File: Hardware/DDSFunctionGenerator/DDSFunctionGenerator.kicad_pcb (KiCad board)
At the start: 2 copper layers, 80 x 65 mm, 156 parts, among them J1 Conn_Coaxial, J2 USB_B_Micro, J3 DG128-5.0-02P-14-00A, J4 Conn_01x02_Female, J5 Conn_Coaxial, J6 Conn_Coaxial, J7 Conn_01x04_Male, J8 Conn_01x04_Female, J9 Conn_01x04_Female, Q1 Q_NPN_BEC, Q2 Q_NPN_BEC, Q3 Q_NPN_BEC, SW1 EN11-VSB1AQ15, T1 Transformer_1P_1S, U1 TC1107-3.3VOA, U2 L78L08_SOT89, U3 L78L33_SO8, U4 AD9832, U5 STM32F030K6Tx, U6 FT200XD, U7 AD8325, U8 MCP3425A0T-ECH, X1 XO91, Y1 20MHz

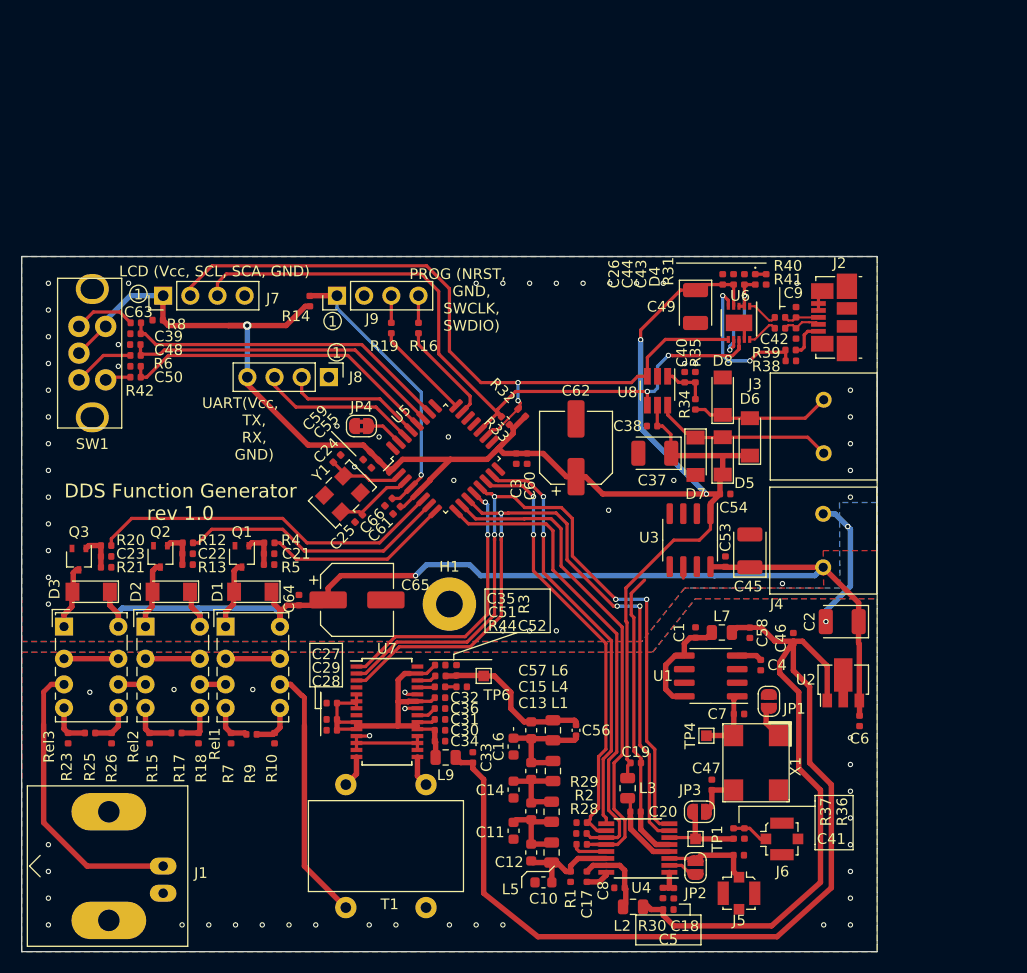
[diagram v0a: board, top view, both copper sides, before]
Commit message: move to raspbbery pico, first draft
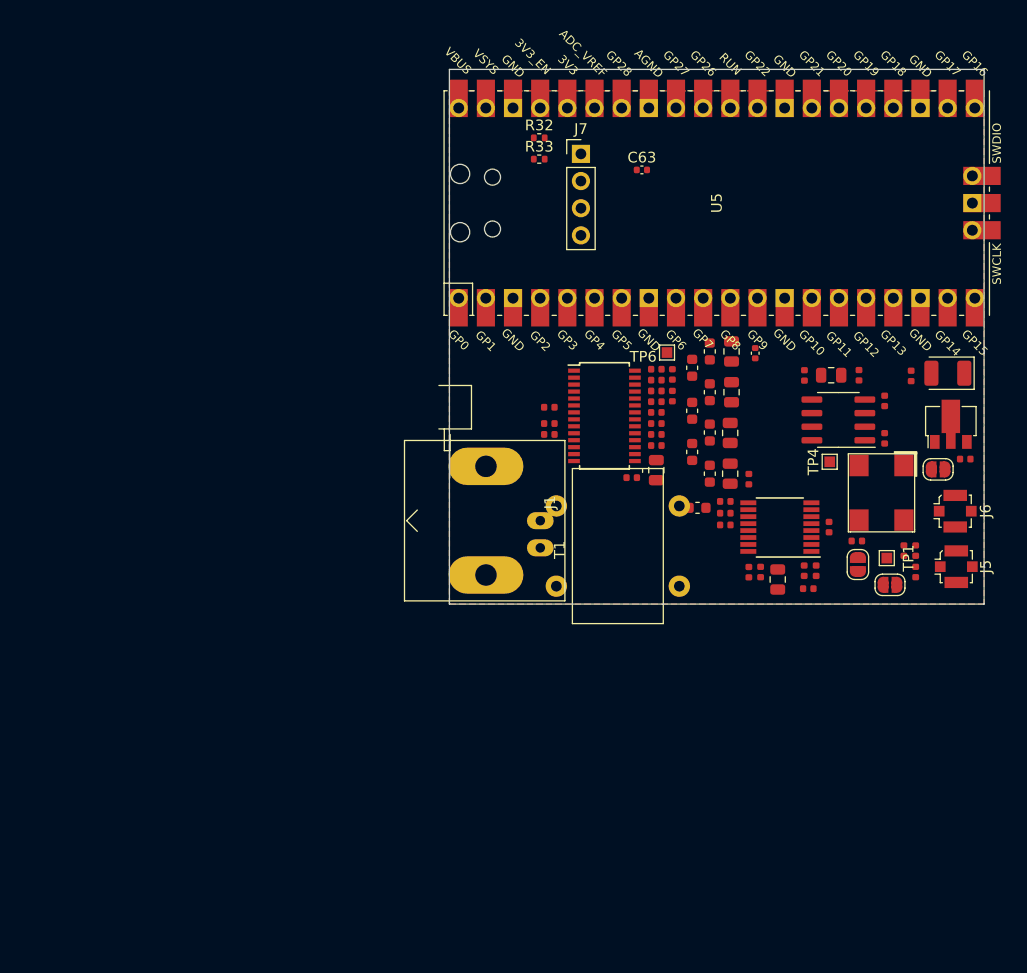
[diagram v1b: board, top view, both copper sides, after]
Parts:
- removed C19, C26, C3, C38, C43, C44, C50, C53, C54, C55, C59, C60, C61, C64, C66: 100n, Capacitor_SMD:C_0402_1005Metric
- removed C21, C22, C23, C40: 1n, Capacitor_SMD:C_0402_1005Metric
- removed C24, C25: 8p2, Capacitor_SMD:C_0402_1005Metric
- removed C37, C49: 47u/6V3, Capacitor_Tantalum_SMD:CP_EIA-3528-21_Kemet-B
- removed C39, C48: 10n, Capacitor_SMD:C_0402_1005Metric
- removed C42, C9: 47p, Capacitor_SMD:C_0402_1005Metric
- removed C45: 47u/10V, Capacitor_Tantalum_SMD:CP_EIA-3528-21_Kemet-B
- removed C62, C65: 220u, Capacitor_SMD:CP_Elec_6.3x5.8
- removed D1, D2, D3, D5, D6, D7, D8: D, Diode_SMD:D_MiniMELF
- removed D4: LED, LED_SMD:LED_0402_1005Metric
- removed H1: MountingHole_Pad, MountingHole:MountingHole_2.5mm_Pad
- removed J2: USB_B_Micro, Connector_USB:USB_Micro-B_Molex_47346-0001
- removed J3: DG128-5.0-02P-14-00A, DDSFunctionGenerator:DG128-5.0-02P-14-00A
- removed J4: Conn_01x02_Female, DDSFunctionGenerator:DG128-5.0-02P-14-00A
- removed J8, J9: Conn_01x04_Female, Connector_PinHeader_2.54mm:PinHeader_1x04_P2.54mm_Vertical
- removed JP4: Jumper_NC_Small, Jumper:SolderJumper-2_P1.3mm_Bridged2Bar_RoundedPad1.0x1.5mm
- removed L3: 10u, Inductor_SMD:L_0805_2012Metric
- removed Q1, Q2, Q3: Q_NPN_BEC, Package_TO_SOT_SMD:SOT-323_SC-70
- removed R10, R15, R18, R23, R26, R7: 53R6, Resistor_SMD:R_0402_1005Metric
- removed R12, R20, R4: 2k2, Resistor_SMD:R_0402_1005Metric
- removed R13, R14, R21, R35, R39, R5: 10k, Resistor_SMD:R_0402_1005Metric
- removed R16, R19: 220R, Resistor_SMD:R_0402_1005Metric
- removed R17, R25, R9: 1k, Resistor_SMD:R_0402_1005Metric
- removed R31: 120R, Resistor_SMD:R_0402_1005Metric
- removed R34: 0R, Resistor_SMD:R_0402_1005Metric
- removed R38: 4k7, Resistor_SMD:R_0402_1005Metric
- removed R40, R41: 27R, Resistor_SMD:R_0402_1005Metric
- removed R42, R6, R8: 100R, Resistor_SMD:R_0402_1005Metric
- removed Rel1, Rel2, Rel3: RSM850B-6112-85-1005, Relay_THT:Relay_DPDT_Omron_G6K-2P-Y
- removed SW1: EN11-VSB1AQ15, DDSFunctionGenerator:EN11-VNB1BQ15
- removed U3: L78L33_SO8, Package_SO:SOIC-8_3.9x4.9mm_P1.27mm
- removed U6: FT200XD, Package_DFN_QFN:DFN-10-1EP_3x3mm_P0.5mm_EP1.55x2.48mm
- removed U8: MCP3425A0T-ECH, Package_TO_SOT_SMD:SOT-23-6_Handsoldering
- removed Y1: 20MHz, Oscillator:Oscillator_SMD_EuroQuartz_XO53-4Pin_5.0x3.2mm
- U5: value STM32F030K6Tx -> RP2040; footprint Package_QFP:LQFP-32_7x7mm_P0.8mm -> MCU_RaspberryPi_and_Boards:RPi_Pico_SMD_TH
- moved J1 47.8 mm to (113.5, 94.7)
- moved C63 47.4 mm to (123.0, 61.9), turned to 0 degrees
- moved J7 41.3 mm to (117.3, 60.4), turned to 0 degrees
- moved R1 40.7 mm to (133.0, 90.8)
- moved C12 39.2 mm to (129.4, 90.3)
- moved L1 39.2 mm to (131.3, 86.5)
- moved L5 39.2 mm to (131.3, 90.3)
- moved L4 39.2 mm to (131.4, 82.7)
- moved L6 39.2 mm to (131.4, 78.9)
- moved C11 39.2 mm to (127.7, 88.3)
- moved C13 39.2 mm to (129.4, 86.5)
- moved C14 39.2 mm to (127.7, 84.4)
- moved C15 39.2 mm to (129.4, 82.7)
- moved C16 39.2 mm to (127.7, 80.4)
- moved C57 39.2 mm to (129.4, 78.9)
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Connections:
- C20 pad 1: Net-(C20-Pad1) -> 5V_DIGITAL
- J1 pad 1: Net-(J1-Pad1) -> (no net)
- T1 pad 3: RF_FROM_AMPLIFIER -> (no net)
- U4 pad 4: Net-(C20-Pad1) -> 5V_DIGITAL
- U4 pad 9: FSYNC -> (no net)
- U5 pad 1: 5V_DIGITAL -> unconnected-(U5-Pad1)
- U5 pad 10: PSEL0 -> unconnected-(U5-Pad10)
- U5 pad 11: SPI1_SCK -> unconnected-(U5-Pad11)
- U5 pad 12: SPI1_CS_AMPLIFIER -> unconnected-(U5-Pad12)
- U5 pad 13: SPI1_MOSI -> unconnected-(U5-Pad13)
- U5 pad 14: FSELECT -> unconnected-(U5-Pad14)
- U5 pad 15: FSYNC -> unconnected-(U5-Pad15)
- U5 pad 16: GND -> unconnected-(U5-Pad16)
- U5 pad 17: 5V_DIGITAL -> unconnected-(U5-Pad17)
- U5 pad 18: (no net) -> unconnected-(U5-Pad18)
- U5 pad 19: SCL -> unconnected-(U5-Pad19)
- U5 pad 2: Net-(C24-Pad2) -> unconnected-(U5-Pad2)
- U5 pad 20: SDA -> unconnected-(U5-Pad20)
- U5 pad 21: (no net) -> unconnected-(U5-Pad21)
- U5 pad 22: (no net) -> unconnected-(U5-Pad22)
- U5 pad 23: /Microcontroller/SWDIO -> unconnected-(U5-Pad23)
- U5 pad 24: /Microcontroller/SWCLK -> unconnected-(U5-Pad24)
- U5 pad 25: (no net) -> unconnected-(U5-Pad25)
- U5 pad 26: ROT_A -> unconnected-(U5-Pad26)
- U5 pad 27: ROT_A -> unconnected-(U5-Pad27)
- U5 pad 28: ROT_S -> unconnected-(U5-Pad28)
- U5 pad 29: /Microcontroller/USART_TX -> unconnected-(U5-Pad29)
- U5 pad 3: Net-(C25-Pad2) -> unconnected-(U5-Pad3)
- U5 pad 30: /Microcontroller/USART_RX -> unconnected-(U5-Pad30)
- U5 pad 31: Net-(JP4-Pad2) -> unconnected-(U5-Pad31)
- U5 pad 32: GND -> unconnected-(U5-Pad32)
- U5 pad 4: /Microcontroller/NRST -> unconnected-(U5-Pad4)
- U5 pad 5: 5V_DIGITAL -> unconnected-(U5-Pad5)
- U5 pad 6: REL_3 -> unconnected-(U5-Pad6)
- U5 pad 7: REL_2 -> unconnected-(U5-Pad7)
- U5 pad 8: REL_1 -> unconnected-(U5-Pad8)
- U5 pad 9: PSEL1 -> unconnected-(U5-Pad9)
- U7 pad 1: SPI1_CS_AMPLIFIER -> (no net)
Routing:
- net 5V_DIGITAL: track 175.4 -> 0.00 mm, vias 3 -> 0
- net 5V_ANALOG: track 132.0 -> 0.00 mm
- net 9V: track 112.2 -> 0.00 mm, vias 1 -> 0
- net SPI1_SCK: track 70.7 -> 0.00 mm, vias 4 -> 0
- net SPI1_MOSI: track 70.7 -> 0.00 mm, vias 4 -> 0
- net SCL: track 69.2 -> 0.00 mm, vias 2 -> 0
- net SDA: track 68.1 -> 0.00 mm, vias 2 -> 0
- net ROT_A: track 61.3 -> 0.00 mm
- net GND: track 60.7 -> 0.00 mm, vias 75 -> 0
- net PSEL0: track 46.5 -> 0.00 mm
- net PSEL1: track 44.8 -> 0.00 mm
- net FSELECT: track 41.2 -> 0.00 mm, vias 2 -> 0
- net FSYNC: track 39.3 -> 0.00 mm, vias 2 -> 0
- net Net-(C27-Pad1): track 34.4 -> 0.00 mm
- net REL_3: track 33.2 -> 0.00 mm
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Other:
- board size 80 x 65 mm -> 50 x 50 mm
- board text removed: "1"
- board text removed: "DDS Function Generator rev 1.0"
- board text removed: "LCD (Vcc, SCL, SCA, GND)"
- board text removed: "PROG (NRST, GND, SWCLK, SWDIO)"
- board text removed: "UART(Vcc, TX, RX, GND)"
